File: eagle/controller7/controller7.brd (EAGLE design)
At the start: 30 x 65 mm, 84 parts, among them IC1 ILD213T, IC2 ILD213T, Q1 2.5A/30V, Q2 200mA/50V, U2 MP2307, U3 MP2307, X1 1501_04, X2 ZX62D-B-5PA8

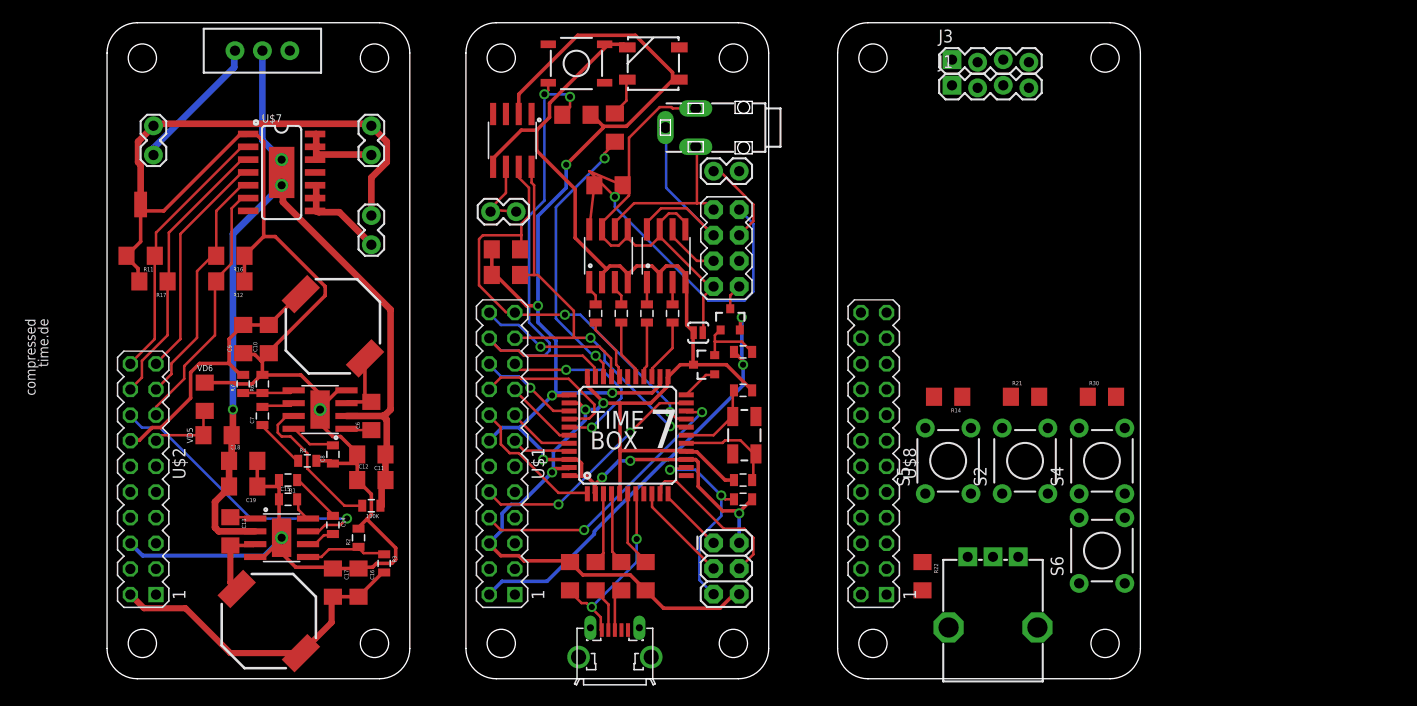
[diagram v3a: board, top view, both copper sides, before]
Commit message: controller7: power board finished
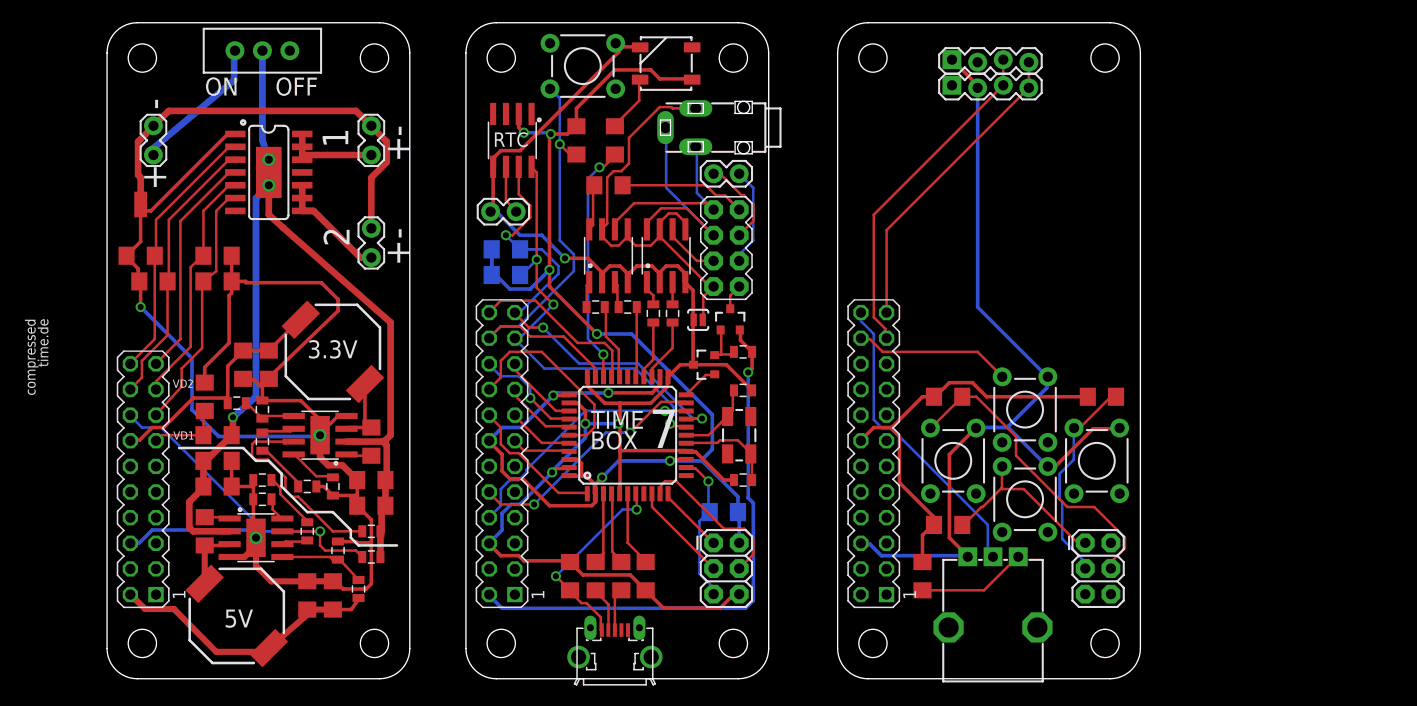
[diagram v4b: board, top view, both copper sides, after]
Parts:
- removed 100K: 6.8k, SparkFun-Resistors:0805
- added J6: (no value), SparkFun-Connectors:2X3
- added R23, R24: 100K, SparkFun-Resistors:0805
- RRST: device SparkFun-Passives:0805 -> SparkFun-Passives:1206
- S1: device SparkFun-Retired:TACTILE-SWITCH-SMD -> SparkFun-Retired:TACTILE-PTH
- moved S6 15.9 mm to (91.4, 26.7)
- moved R21 14.8 mm to (83.8, 15.2)
- moved S2 3.81 mm to (91.4, 17.8)
- moved R3 3.59 mm to (25.4, 8.89)
- moved L2 3.22 mm to (13.3, 6.22)
- moved C8 3.18 mm to (22.9, 19.1)
- moved C16 2.84 mm to (22.9, 8.26)
- moved C17 2.84 mm to (20.3, 8.26)
- moved C14 2.62 mm to (20.3, 14.6)
- moved C10 2.54 mm to (16.5, 31.1)
- moved C11 2.54 mm to (26.7, 19.7)
- moved C9 2.54 mm to (14.0, 31.1)
- moved U2 2.54 mm to (21.6, 24.1)
- moved C18 2.54 mm to (11.4, 21.6)
- moved C19 2.54 mm to (11.4, 19.1)
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- renumbered VD5 to VD1, VD6 to VD2
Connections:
- removed net N$38: R14.1, S5.2
- removed net N$39: R30.2, S4.2
- removed net N$40: R21.2, S2.2
- new net DB_MISO: J6.1, R21.2, S2.2
- new net DB_MOSI: J6.4, R14.1, S5.2
- new net DB_RST: J6.5
- new net DB_SCK: J6.3, R30.2, S4.2
- new net N$45: J6.2
- new net N$46: J6.6
- net BATT_VCC: now also R23.1, R24.1; no longer 100K.1
- net CAM_EN1: now also U$3.37; no longer U$3.36
- net N$2: now also R23.2; no longer 100K.2
- net PB_BUCK_EN: now also R24.2
- net PROFET1: now also U$3.39; no longer U$3.37
- net PROFET2: now also U$3.36; no longer U$3.38
- net PROFET3: now also U$3.38; no longer U$3.39
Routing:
- net 3.3V: track 0.00 -> 85.3 mm
- net VCC_2: track 0.00 -> 41.1 mm
- net DB_SCL: track 0.00 -> 33.5 mm
- net DB_MOSI: track 0.00 -> 31.1 mm
- net DB_SDA: track 0.00 -> 30.6 mm
- net DB_ANALOG_IO: track 0.00 -> 30.1 mm
- net GND-ISO: track 148.9 -> 172.1 mm, vias 0 -> 1
- net N$16: track 34.8 -> 12.6 mm, vias 1 -> 0
- net DB_SCK: track 0.00 -> 21.0 mm
- net DB_MISO: track 0.00 -> 18.1 mm
- net DB_BTN: track 0.00 -> 15.6 mm
- net PROFET2: track 18.9 -> 7.65 mm, vias 2 -> 0
- net CONV_5V: track 43.7 -> 54.8 mm, vias 2 -> 1
- net N$43: track 0.00 -> 10.9 mm
- net N$6: track 0.00 -> 9.79 mm
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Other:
- board text added: "+"
- board text added: "-"
- board text added: "1"
- board text added: "2"
- board text added: "3.3V"
- board text added: "5V"
- board text added: "CONTROLLER7"
- board text added: "OFF"
- board text added: "ON"
- board text added: "POWERBOARD1"
- board text added: "RTC"

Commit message: controller7: controllerboard nearly finished
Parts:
- moved R9 12.5 mm to (51.4, 37.5), turned to 0 degrees
- moved R8 10.2 mm to (50.2, 40.0), turned to 180 degrees
- moved RTC2 8.98 mm to (41.9, 44.5)
- moved J4 8.34 mm to (40.6, 54.6), turned to 270 degrees
- moved RRST 8.13 mm to (56.5, 10.2), flipped to the top, turned to 90 degrees
- moved R5 2.84 mm to (44.5, 54.6), turned to 90 degrees
- moved R13 1.27 mm to (51.4, 48.9)
- moved R_LED 1.27 mm to (52.1, 53.3)
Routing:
- net VBAT1: track 4.87 -> 20.1 mm
- net PROFET1: track 20.2 -> 9.80 mm
- net VCC: track 140.4 -> 149.3 mm, vias 8 -> 5
- net LED: track 24.0 -> 32.5 mm
- net RST: track 15.0 -> 23.0 mm
- net GND: track 159.6 -> 165.7 mm, vias 4 -> 3
- net ANALOG_IO: track 17.4 -> 15.9 mm, vias 0 -> 1
- net N$22: track 19.9 -> 21.4 mm
- net N$16: track 12.6 -> 11.3 mm
- net PROFET2: track 7.65 -> 8.80 mm
- net TX: track 24.3 -> 23.4 mm, vias 2 -> 1
- net SCL: track 44.4 -> 43.5 mm, vias 3 -> 2
- net SCK: track 9.94 -> 10.6 mm
- net N$7: track 5.67 -> 5.15 mm
- net N$18: track 4.65 -> 5.18 mm
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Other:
- board text added: "GND"

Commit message: controller7: controllerboard finished
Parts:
- added C1: 0.1uF (low leakage), SparkFun-Capacitors:1206
- added F2: PTCSMD-W, SparkFun-PowerIC:PTC-1206-WIDE
- moved RTC2 1.27 mm to (43.2, 44.5)
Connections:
- removed net FOO15: U$3.12
- removed net FOO8: U$3.8
- removed net VBAT1: J4.1, RTC2.6
- new net N$38: F2.1, X2.1
- new net N$39: C1.1, J4.1, RTC2.6
- net GND: now also C1.2
- net N$22: now also F2.2; no longer X2.1
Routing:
- net N$39: track 0.00 -> 21.5 mm
- net VBAT1: track 20.1 -> 0.00 mm
- net N$38: track 0.00 -> 7.99 mm
- net N$22: track 21.4 -> 20.2 mm
- net SCL: track 43.5 -> 42.7 mm
- net VCC: track 149.3 -> 148.7 mm
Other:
- board text added: "BOARD1"
- board text added: "COIN CELL"

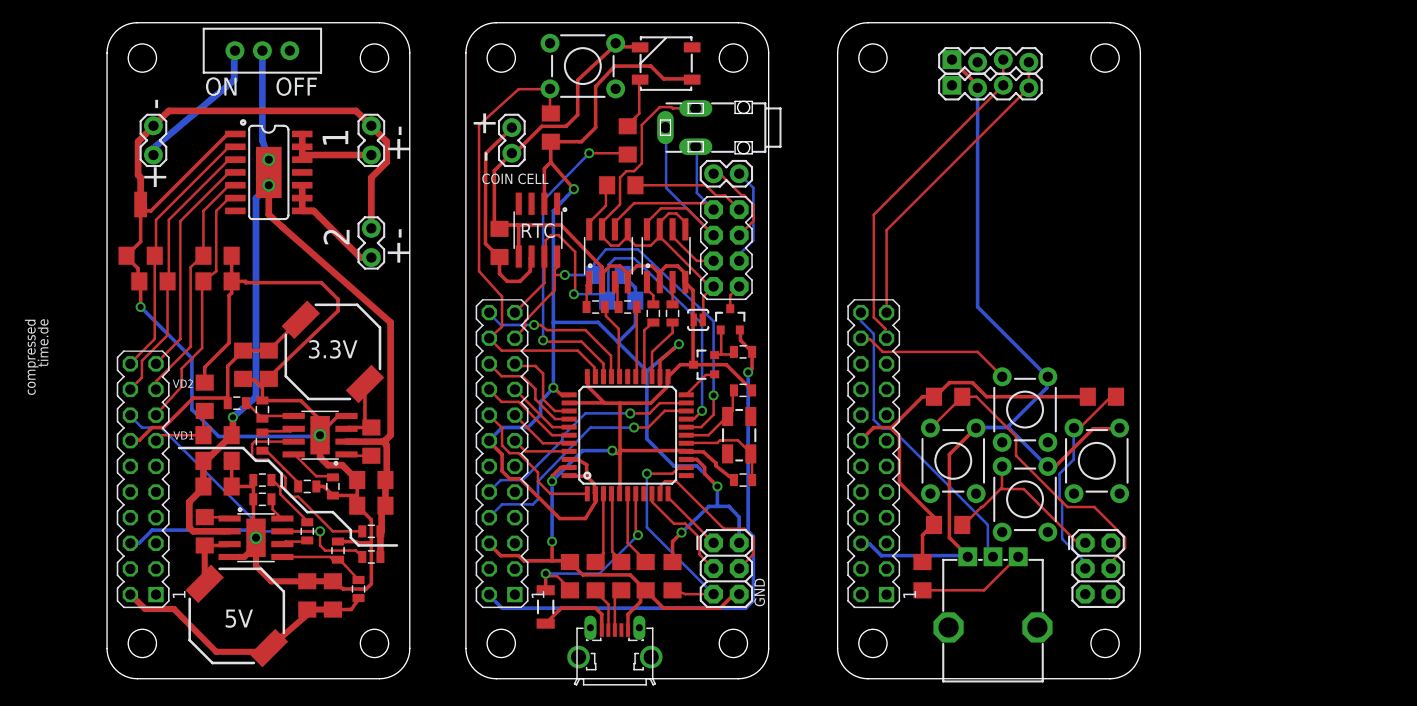
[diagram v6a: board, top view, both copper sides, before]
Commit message: controller7: values for voltage divider resistors
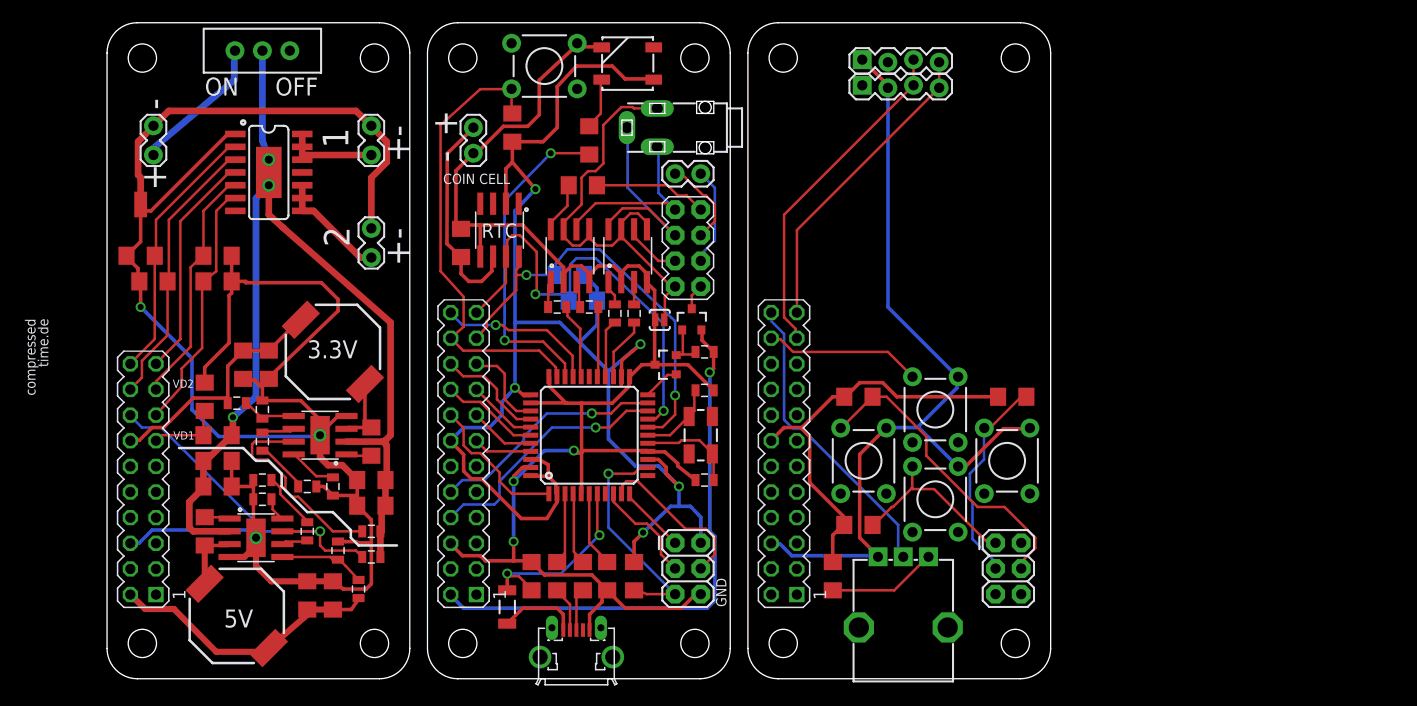
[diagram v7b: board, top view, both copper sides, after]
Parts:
- VD1: value (none) -> 10k
- VD2: value (none) -> 6.2k
- moved J6 8.89 mm to (88.5, 13.5)
- moved R22 8.89 mm to (72.4, 10.2)
- moved R30 8.89 mm to (90.2, 27.9)
- moved RV1 8.89 mm to (79.4, 5.08)
- moved S2 8.89 mm to (82.5, 17.8)
- moved S4 8.89 mm to (89.7, 21.6)
- moved S5 8.89 mm to (75.4, 21.6)
- moved S6 8.89 mm to (82.5, 26.7)
- moved U$8 8.89 mm to (94.0, 0.00)
- moved J1 8.89 mm to (75.3, 58.7)
- moved J3 8.89 mm to (75.3, 61.2)
- moved R14 8.89 mm to (74.9, 27.9)
- moved R21 8.89 mm to (74.9, 15.2)
- moved U$1 3.81 mm to (62.2, 0.00)
- moved C2 3.81 mm to (50.0, 10.2)
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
